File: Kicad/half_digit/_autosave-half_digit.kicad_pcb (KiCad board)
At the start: 2 copper layers, 106.7 x 152.4 mm, 41 parts, among them J1 CONN_8, J2 CONN_8, J3 CONN_8, J4 CONN_8, J5 CONN_12, J6 CONN_12, J7 CONN_12, J8 CONN_12, J9 BARREL_JACK, U1 TLC5917, U2 AOZ1280, X1 MTHOLE, X2 MTHOLE, X3 MTHOLE, X4 MTHOLE

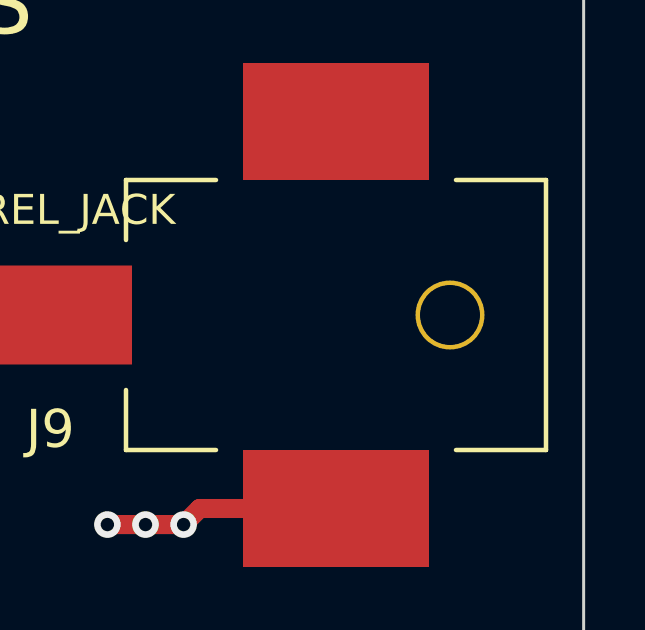
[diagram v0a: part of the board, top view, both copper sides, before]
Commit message: Rough draft of half digit layout
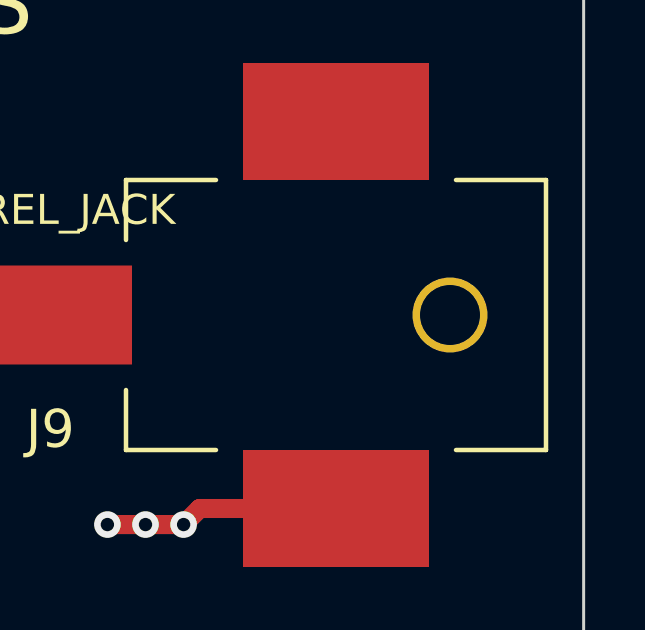
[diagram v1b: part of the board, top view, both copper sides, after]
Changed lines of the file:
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@@
     (mod_text_size 1.016 1.016)
     (mod_text_width 0.381)
-    (pad_size 1.524 1.524)
-    (pad_drill 1.016)
+    (pad_size 2.5 2.5)
+    (pad_drill 2)
     (pad_to_mask_clearance 0.1778)
     (pad_to_paste_clearance -0.0635)
@@
     )
   )
-  (module PJ-036AH-SMT (layer F.Cu)
-    (at 167.005 205.74 180)
-    (fp_text reference J9 (at 9.525 -3.81 180) (layer F.SilkS)
-      (effects (font (size 1.27 1.27) (thickness 0.254)))
-    )
-    (fp_text value BARREL_JACK (at 10 3.5 180) (layer F.SilkS)
-      (effects (font (size 1 1) (thickness 0.15)))
-    )
-    (fp_line (start 7 -2.5) (end 7 -4.5) (layer F.SilkS) (width 0.15))
-    (fp_line (start 7 -4.5) (end 4 -4.5) (layer F.SilkS) (width 0.15))
-    (fp_line (start 4 4.5) (end 7 4.5) (layer F.SilkS) (width 0.15))
-    (fp_line (start 7 4.5) (end 7 2.5) (layer F.SilkS) (width 0.15))
-    (fp_line (start -7 4.5) (end -7 -4.5) (layer F.SilkS) (width 0.15))
-    (fp_line (start -7 -4.5) (end -4 -4.5) (layer F.SilkS) (width 0.15))
-    (fp_line (start -7 4.5) (end -4 4.5) (layer F.SilkS) (width 0.15))
-    (pad 1 smd rect (at 9 0 180) (size 4.4 3.3)
-      (layers F.Cu F.Paste F.Mask)
-      (net 17 N-0000021)
-    )
-    (pad 2 smd rect (at 0 -6.45 180) (size 6.2 3.9)
-      (layers F.Cu F.Paste F.Mask)
-      (net 8 GND)
-    )
-    (pad 3 smd rect (at 0 6.45 180) (size 6.2 3.9)
-      (layers F.Cu F.Paste F.Mask)
-    )
-    (pad "" thru_hole circle (at -3.8 0 180) (size 2.3 2.3) (drill 2)
-      (layers *.Cu *.Mask F.SilkS)
-    )
-  )
   (module HEADER_12X1 (layer F.Cu)
     (at 135.255 74.295 180)
@@
       (layers *.Cu *.Mask F.SilkS)
     )
+  )
+  (module PJ-036AH-SMT (layer F.Cu)
+    (at 167.005 205.74 180)
+    (fp_text reference J9 (at 9.525 -3.81 180) (layer F.SilkS)
+      (effects (font (size 1.27 1.27) (thickness 0.254)))
+    )
+    (fp_text value BARREL_JACK (at 10 3.5 180) (layer F.SilkS)
+      (effects (font (size 1 1) (thickness 0.15)))
+    )
+    (fp_line (start 7 -2.5) (end 7 -4.5) (layer F.SilkS) (width 0.15))
+    (fp_line (start 7 -4.5) (end 4 -4.5) (layer F.SilkS) (width 0.15))
+    (fp_line (start 4 4.5) (end 7 4.5) (layer F.SilkS) (width 0.15))
+    (fp_line (start 7 4.5) (end 7 2.5) (layer F.SilkS) (width 0.15))
+    (fp_line (start -7 4.5) (end -7 -4.5) (layer F.SilkS) (width 0.15))
+    (fp_line (start -7 -4.5) (end -4 -4.5) (layer F.SilkS) (width 0.15))
+    (fp_line (start -7 4.5) (end -4 4.5) (layer F.SilkS) (width 0.15))
+    (pad 1 smd rect (at 9 0 180) (size 4.4 3.3)
+      (layers F.Cu F.Paste F.Mask)
+      (net 17 N-0000021)
+    )
+    (pad 2 smd rect (at 0 -6.45 180) (size 6.2 3.9)
+      (layers F.Cu F.Paste F.Mask)
+      (net 8 GND)
+    )
+    (pad 3 smd rect (at 0 6.45 180) (size 6.2 3.9)
+      (layers F.Cu F.Paste F.Mask)
+    )
+    (pad "" thru_hole circle (at -3.8 0 180) (size 2.5 2.5) (drill 2)
+      (layers *.Cu *.Mask F.SilkS)
+    )
